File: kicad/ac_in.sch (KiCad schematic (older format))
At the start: 31 parts, among them J701 tblock, U702 R-78B3.3-2.0, U706 AP2114H-1.2TRG1

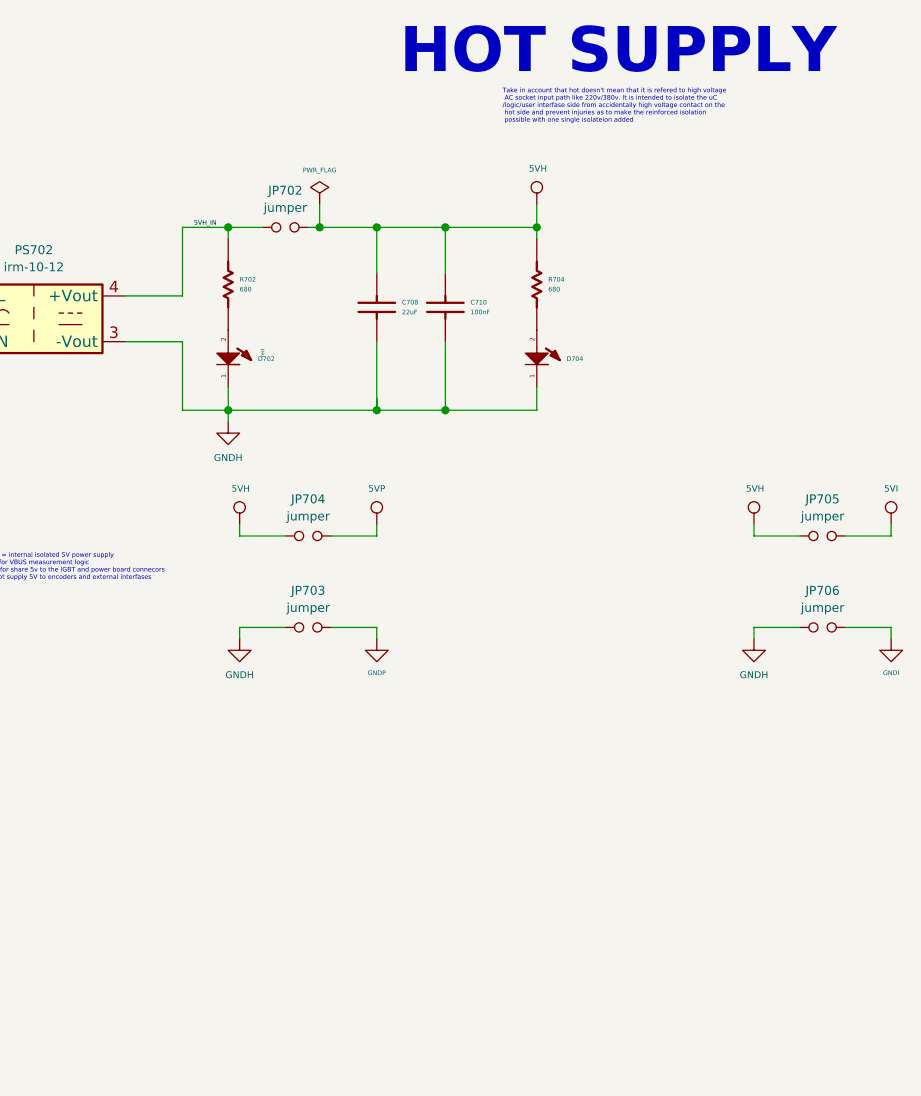
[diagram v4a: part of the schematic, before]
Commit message: added sloted holes everyware
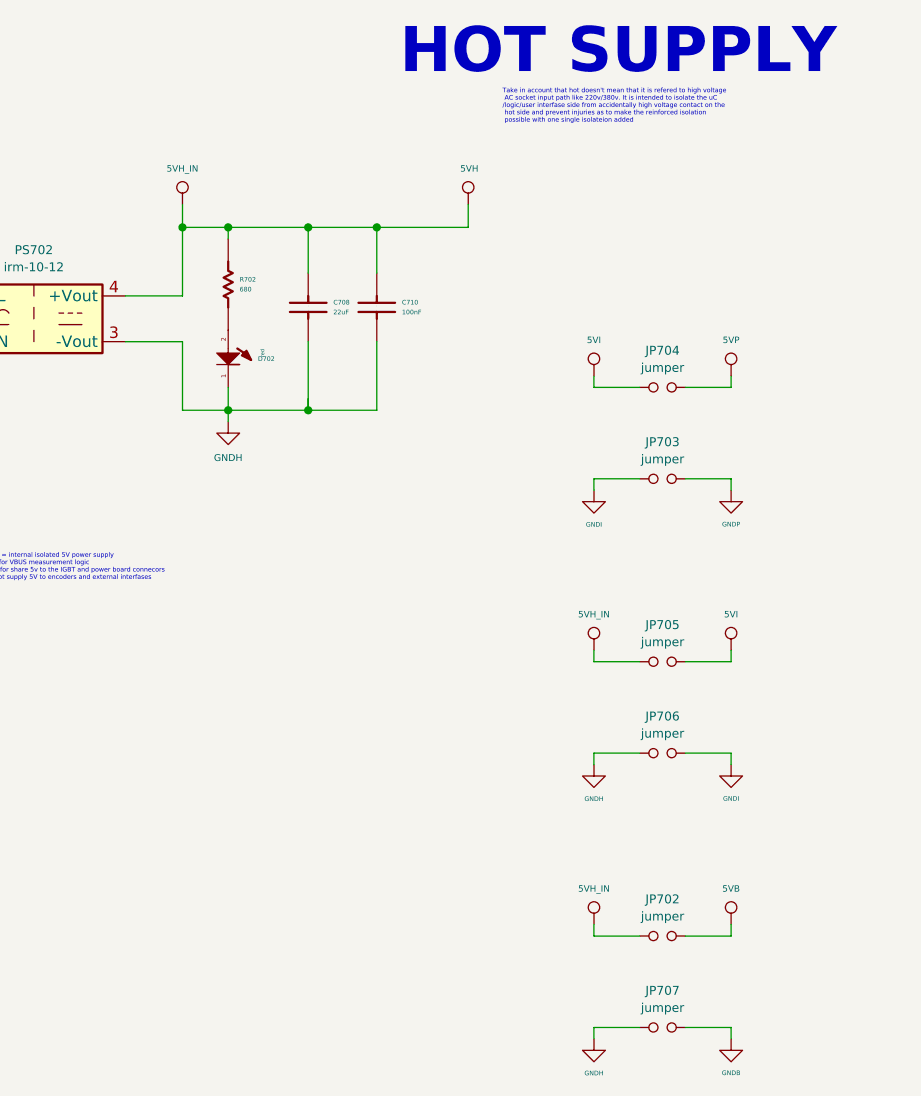
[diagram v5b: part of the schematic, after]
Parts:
- removed D704: red, servo:LED_0603_1608Metric, symbol servo:LED_A2_K1
- removed R704: 680, Resistor_SMD:R_0603_1608Metric, symbol servo:Resistor
- added JP707: jumper, Resistor_SMD:R_1806_4516Metric_Pad1.57x1.80mm_HandSolder, symbol servo:jumper
- JP702: footprint servo:SolderJumper-2_P1.3mm_Open_RoundedPad1.0x1.5mm -> Resistor_SMD:R_1806_4516Metric_Pad1.57x1.80mm_HandSolder
- JP705: footprint servo:wire_bridge_50mm -> Resistor_SMD:R_1806_4516Metric_Pad1.57x1.80mm_HandSolder
- JP706: footprint servo:wire_bridge_60mm -> Resistor_SMD:R_1806_4516Metric_Pad1.57x1.80mm_HandSolder
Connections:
- net labels added: 5VB, GNDB
- wire segments 123 -> 126
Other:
- moved on the sheet: C708, C710, JP703, JP704, JP705

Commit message: serigrafia...
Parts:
- added D703, D704: Z1SMAxxx, servo:D_SMA, symbol Diode:Z1SMAxxx
- R701, R702, R705, R706: footprint Resistor_SMD:R_0603_1608Metric -> servo:R_0603_1608Metric
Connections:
- wire segments 126 -> 134
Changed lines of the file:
@@
 F 0 "R705" V 5978 6000 20  0000 L CNN
 F 1 "680" V 6021 6000 20  0000 L CNN
-F 2 "Resistor_SMD:R_0603_1608Metric" H 5500 5850 60  0001 C CNN
+F 2 "servo:R_0603_1608Metric" H 5500 5850 60  0001 C CNN
 F 3 "" H 5600 5950 60  0001 C CNN
 F 4 "680" V -6400 6350 60  0001 C CNN "ValueDisplayed"
@@
 F 0 "R706" V 8078 6000 20  0000 L CNN
 F 1 "680" V 8121 6000 20  0000 L CNN
-F 2 "Resistor_SMD:R_0603_1608Metric" H 7600 5850 60  0001 C CNN
+F 2 "servo:R_0603_1608Metric" H 7600 5850 60  0001 C CNN
 F 3 "" H 7700 5950 60  0001 C CNN
 F 4 "680" V -4300 6350 60  0001 C CNN "ValueDisplayed"
@@
 F 0 "R701" V 3528 5900 20  0000 L CNN
 F 1 "680" V 3571 5900 20  0000 L CNN
-F 2 "Resistor_SMD:R_0603_1608Metric" H 3050 5750 60  0001 C CNN
+F 2 "servo:R_0603_1608Metric" H 3050 5750 60  0001 C CNN
 F 3 "" H 3150 5850 60  0001 C CNN
 F 4 "680" V -8850 6250 60  0001 C CNN "ValueDisplayed"
@@
 F 0 "R702" V 12278 5850 20  0000 L CNN
 F 1 "680" V 12321 5850 20  0000 L CNN
-F 2 "Resistor_SMD:R_0603_1608Metric" H 11800 5700 60  0001 C CNN
+F 2 "servo:R_0603_1608Metric" H 11800 5700 60  0001 C CNN
 F 3 "" H 11900 5800 60  0001 C CNN
 F 4 "680" V -100 6200 60  0001 C CNN "ValueDisplayed"
@@
 Wire Wire Line
 	12650 6050 12650 6350
+$Comp
+L Diode:Z1SMAxxx D704
+U 1 1 5E3BEF67
+P 14850 6450
+F 0 "D704" V 14804 6529 50  0000 L CNN
+F 1 "Z1SMAxxx" V 14895 6529 50  0000 L CNN
+F 2 "servo:D_SMA" H 14850 6275 50  0001 C CNN
+F 3 "https://diotec.com/tl_files/diotec/files/pdf/datasheets/z1sma1.pdf" H 14850 6450 50  0001 C CNN
+	1    14850 6450
+	0    1    1    0
+$EndComp
+Wire Wire Line
+	14500 6250 14850 6250
+Wire Wire Line
+	14850 6250 14850 6300
+Connection ~ 14500 6250
+Wire Wire Line
+	14500 6650 14850 6650
+Wire Wire Line
+	14850 6650 14850 6600
+Connection ~ 14500 6650
+$Comp
+L Diode:Z1SMAxxx D703
+U 1 1 5E3CE25B
+P 14800 7650
+F 0 "D703" V 14754 7729 50  0000 L CNN
+F 1 "Z1SMAxxx" V 14845 7729 50  0000 L CNN
+F 2 "servo:D_SMA" H 14800 7475 50  0001 C CNN
+F 3 "https://diotec.com/tl_files/diotec/files/pdf/datasheets/z1sma1.pdf" H 14800 7650 50  0001 C CNN
+	1    14800 7650
+	0    1    1    0
+$EndComp
+Wire Wire Line
+	14500 7450 14800 7450
+Wire Wire Line
+	14800 7450 14800 7500
+Connection ~ 14500 7450
+Wire Wire Line
+	14500 7850 14800 7850
+Wire Wire Line
+	14800 7850 14800 7800
+Connection ~ 14500 7850
 $EndSCHEMATC

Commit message: serigraphi, improve of nets. change of soic 8 footprint
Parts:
- U702: footprint Converter_DCDC:Converter_DCDC_RECOM_R-78E-0.5_THT -> servo:Converter_DCDC_RECOM_R-78E-0.5_THT
- U706: footprint Package_TO_SOT_SMD:SOT-223 -> servo:SOT-223
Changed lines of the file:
@@
 F 0 "U702" H 5050 5775 39  0000 C CNN
 F 1 "R-78B3.3-2.0" H 5200 5775 39  0000 L CNN
-F 2 "Converter_DCDC:Converter_DCDC_RECOM_R-78E-0.5_THT" H 5250 5400 50  0001 L CIN
+F 2 "servo:Converter_DCDC_RECOM_R-78E-0.5_THT" H 5250 5400 50  0001 L CIN
 F 3 "../doc/datasheets/R-78B-2.0.pdf" H 5050 5775 50  0001 C CNN
 	1    5200 5650
@@
 F 0 "U706" H 6850 6091 39  0000 C CNN
 F 1 "AP2114H-1.2TRG1" H 6850 6016 39  0000 C CNN
-F 2 "Package_TO_SOT_SMD:SOT-223" H 6950 6375 50  0001 C CNN
+F 2 "servo:SOT-223" H 6950 6375 50  0001 C CNN
 F 3 "../doc/datasheets/AP2114.pdf" H 6900 6150 50  0001 C CNN
 	1    6850 5750

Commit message: more serigraphy and now begin with planes
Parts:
- JP702, JP705, JP706, JP707: footprint Resistor_SMD:R_1806_4516Metric_Pad1.57x1.80mm_HandSolder -> servo:R_1806_4516Metric_Pad1.57x1.80mm_HandSolder
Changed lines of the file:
@@
 F 0 "JP705" H 14200 7611 39  0000 C CNN
 F 1 "jumper" H 14200 7536 39  0000 C CNN
-F 2 "Resistor_SMD:R_1806_4516Metric_Pad1.57x1.80mm_HandSolder" H 14100 7430 50  0001 C CNN
+F 2 "servo:R_1806_4516Metric_Pad1.57x1.80mm_HandSolder" H 14100 7430 50  0001 C CNN
 F 3 "~" H 14200 7530 50  0001 C CNN
 	1    14200 7450
@@
 F 0 "JP706" H 14200 8011 39  0000 C CNN
 F 1 "jumper" H 14200 7936 39  0000 C CNN
-F 2 "Resistor_SMD:R_1806_4516Metric_Pad1.57x1.80mm_HandSolder" H 14100 7830 50  0001 C CNN
+F 2 "servo:R_1806_4516Metric_Pad1.57x1.80mm_HandSolder" H 14100 7830 50  0001 C CNN
 F 3 "~" H 14200 7930 50  0001 C CNN
 	1    14200 7850
@@
 F 0 "JP702" H 14200 8811 39  0000 C CNN
 F 1 "jumper" H 14200 8736 39  0000 C CNN
-F 2 "Resistor_SMD:R_1806_4516Metric_Pad1.57x1.80mm_HandSolder" H 14100 8630 50  0001 C CNN
+F 2 "servo:R_1806_4516Metric_Pad1.57x1.80mm_HandSolder" H 14100 8630 50  0001 C CNN
 F 3 "~" H 14200 8730 50  0001 C CNN
 	1    14200 8650
@@
 F 0 "JP707" H 14200 9211 39  0000 C CNN
 F 1 "jumper" H 14200 9136 39  0000 C CNN
-F 2 "Resistor_SMD:R_1806_4516Metric_Pad1.57x1.80mm_HandSolder" H 14100 9030 50  0001 C CNN
+F 2 "servo:R_1806_4516Metric_Pad1.57x1.80mm_HandSolder" H 14100 9030 50  0001 C CNN
 F 3 "~" H 14200 9130 50  0001 C CNN
 	1    14200 9050
